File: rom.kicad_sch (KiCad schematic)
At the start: 7 parts, among them U10 28C256, U6 74HC32, U7 74HC14, U8 74HC05, U9 28C256

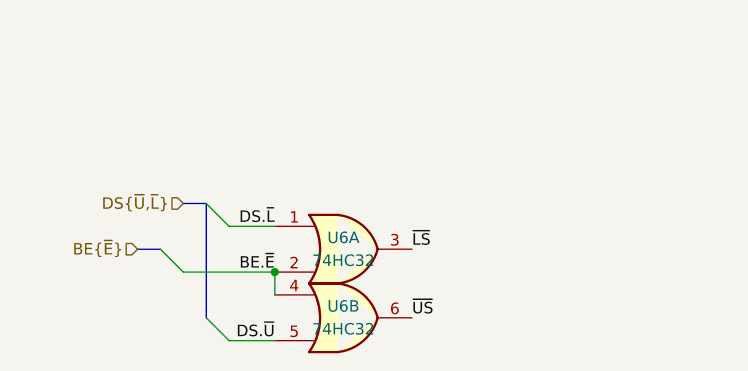
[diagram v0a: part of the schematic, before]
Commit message: finished scheme, footprints not completely assigned yet
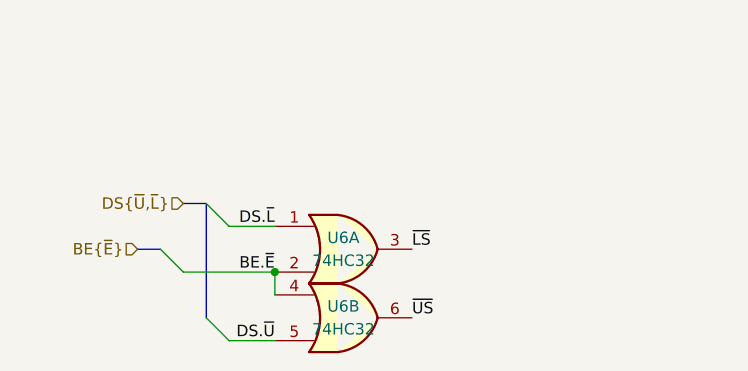
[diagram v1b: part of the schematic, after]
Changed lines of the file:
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@@
 (kicad_sch
-	(version 20231120)
+	(version 20250114)
 	(generator "eeschema")
-	(generator_version "8.0")
+	(generator_version "9.0")
 	(paper "A4")
 	(junction
@@
 	(label "~{US}"
 		(at 83.82 149.86 0)
-		(fields_autoplaced yes)
 		(effects
 			(font
@@
 	(label "DIR.~{R}"
 		(at 142.24 121.92 180)
-		(fields_autoplaced yes)
 		(effects
 			(font
@@
 	(label "A_{14}"
 		(at 205.74 111.76 180)
-		(fields_autoplaced yes)
 		(effects
 			(font
@@
 	(label "A_{12}"
 		(at 142.24 106.68 180)
-		(fields_autoplaced yes)
 		(effects
 			(font
@@
 	(label "A_{9}"
 		(at 205.74 99.06 180)
-		(fields_autoplaced yes)
 		(effects
 			(font
@@
 	(label "~{LS}"
 		(at 142.24 124.46 180)
-		(fields_autoplaced yes)
 		(effects
 			(font
@@
 	(label "D_{3}"
 		(at 162.56 86.36 0)
-		(fields_autoplaced yes)
 		(effects
 			(font
@@
 	(label "A_{7}"
 		(at 142.24 93.98 180)
-		(fields_autoplaced yes)
 		(effects
 			(font
@@
 	(label "BE.~{E}"
 		(at 63.5 76.2 180)
-		(fields_autoplaced yes)
 		(effects
 			(font
@@
 	(label "A_{6}"
 		(at 205.74 91.44 180)
-		(fields_autoplaced yes)
 		(effects
 			(font
@@
 	(label "D_{11}"
 		(at 226.06 86.36 0)
-		(fields_autoplaced yes)
 		(effects
 			(font
@@
 	(label "A_{8}"
 		(at 205.74 96.52 180)
-		(fields_autoplaced yes)
 		(effects
 			(font
@@
 	(label "A_{5}"
 		(at 205.74 88.9 180)
-		(fields_autoplaced yes)
 		(effects
 			(font
@@
 	(label "A_{3}"
 		(at 142.24 83.82 180)
-		(fields_autoplaced yes)
 		(effects
 			(font
@@
 	(label "D_{8}"
 		(at 226.06 78.74 0)
-		(fields_autoplaced yes)
 		(effects
 			(font
@@
 	(label "D_{12}"
 		(at 226.06 88.9 0)
-		(fields_autoplaced yes)
 		(effects
 			(font
@@
 	(label "A_{7}"
 		(at 205.74 93.98 180)
-		(fields_autoplaced yes)
 		(effects
 			(font
@@
 	(label "A_{6}"
 		(at 142.24 91.44 180)
-		(fields_autoplaced yes)
 		(effects
 			(font
@@
 	(label "A_{13}"
 		(at 205.74 109.22 180)
-		(fields_autoplaced yes)
 		(effects
 			(font
@@
 	(label "~{LS}"
 		(at 83.82 142.24 0)
-		(fields_autoplaced yes)
 		(effects
 			(font
@@
 	(label "A_{5}"
 		(at 142.24 88.9 180)
-		(fields_autoplaced yes)
 		(effects
 			(font
@@
 	(label "DIR.~{W}"
 		(at 142.24 119.38 180)
-		(fields_autoplaced yes)
 		(effects
 			(font
@@
 	(label "A_{4}"
 		(at 205.74 86.36 180)
-		(fields_autoplaced yes)
 		(effects
 			(font
@@
 	(label "D_{10}"
 		(at 226.06 83.82 0)
-		(fields_autoplaced yes)
 		(effects
 			(font
@@
 	(label "BE.~{E}"
 		(at 68.58 144.78 180)
-		(fields_autoplaced yes)
 		(effects
 			(font
@@
 	(label "D_{1}"
 		(at 162.56 81.28 0)
-		(fields_autoplaced yes)
 		(effects
 			(font
@@
 	(label "A_{10}"
 		(at 142.24 101.6 180)
-		(fields_autoplaced yes)
 		(effects
 			(font
@@
 	(label "A_{2}"
 		(at 142.24 81.28 180)
-		(fields_autoplaced yes)
 		(effects
 			(font
@@
 	(label "A_{2}"
 		(at 205.74 81.28 180)
-		(fields_autoplaced yes)
 		(effects
 			(font
@@
 	(label "D_{4}"
 		(at 162.56 88.9 0)
-		(fields_autoplaced yes)
 		(effects
 			(font
@@
 	(label "D_{9}"
 		(at 226.06 81.28 0)
-		(fields_autoplaced yes)
 		(effects
 			(font
@@
 	(label "A_{14}"
 		(at 142.24 111.76 180)
-		(fields_autoplaced yes)
 		(effects
 			(font
@@
 	(label "D_{15}"
 		(at 226.06 96.52 0)
-		(fields_autoplaced yes)
 		(effects
 			(font
@@
 	(label "A_{9}"
 		(at 142.24 99.06 180)
-		(fields_autoplaced yes)
 		(effects
 			(font
@@
 	(label "A_{1}"
 		(at 205.74 78.74 180)
-		(fields_autoplaced yes)
 		(effects
 			(font
@@
 	(label "DS.~{L}"
 		(at 68.58 139.7 180)
-		(fields_autoplaced yes)
 		(effects
 			(font
@@
 	(label "DS.~{U}"
 		(at 68.58 152.4 180)
-		(fields_autoplaced yes)
 		(effects
 			(font
@@
 	(label "A_{4}"
 		(at 142.24 86.36 180)
-		(fields_autoplaced yes)
 		(effects
 			(font
@@
 	(label "A_{8}"
 		(at 142.24 96.52 180)
-		(fields_autoplaced yes)
 		(effects
 			(font
@@
 	(label "A_{15}"
 		(at 205.74 114.3 180)
-		(fields_autoplaced yes)
 		(effects
 			(font
@@
 	(label "D_{2}"
 		(at 162.56 83.82 0)
-		(fields_autoplaced yes)
 		(effects
 			(font
@@
 	(label "A_{12}"
 		(at 205.74 106.68 180)
-		(fields_autoplaced yes)
 		(effects
 			(font
@@
 	(label "DIR.~{W}"
 		(at 205.74 119.38 180)
-		(fields_autoplaced yes)
 		(effects
 			(font
@@
 	(label "D_{14}"
 		(at 226.06 93.98 0)
-		(fields_autoplaced yes)
 		(effects
 			(font
@@
 	(label "~{US}"
 		(at 205.74 124.46 180)
-		(fields_autoplaced yes)
 		(effects
 			(font
@@
 	(label "A_{13}"
 		(at 142.24 109.22 180)
-		(fields_autoplaced yes)
 		(effects
 			(font
@@
 	(label "D_{6}"
 		(at 162.56 93.98 0)
-		(fields_autoplaced yes)
 		(effects
 			(font
@@
 	(label "D_{13}"
 		(at 226.06 91.44 0)
-		(fields_autoplaced yes)
 		(effects
 			(font
@@
 	(label "D_{0}"
 		(at 162.56 78.74 0)
-		(fields_autoplaced yes)
 		(effects
 			(font
@@
 	(label "A_{3}"
 		(at 205.74 83.82 180)
-		(fields_autoplaced yes)
 		(effects
 			(font
@@
 	(label "D_{7}"
 		(at 162.56 96.52 0)
-		(fields_autoplaced yes)
 		(effects
 			(font
@@
 	(label "DIR.~{R}"
 		(at 205.74 121.92 180)
-		(fields_autoplaced yes)
 		(effects
 			(font
@@
 	(label "A_{11}"
 		(at 205.74 104.14 180)
-		(fields_autoplaced yes)
 		(effects
 			(font
@@
 	(label "A_{15}"
 		(at 142.24 114.3 180)
-		(fields_autoplaced yes)
 		(effects
 			(font
@@
 	(label "A_{10}"
 		(at 205.74 101.6 180)
-		(fields_autoplaced yes)
 		(effects
 			(font
@@
 	(label "A_{1}"
 		(at 142.24 78.74 180)
-		(fields_autoplaced yes)
 		(effects
 			(font
@@
 	(label "D_{5}"
 		(at 162.56 91.44 0)
-		(fields_autoplaced yes)
 		(effects
 			(font
@@
 	(label "A_{11}"
 		(at 142.24 104.14 180)
-		(fields_autoplaced yes)
 		(effects
 			(font
@@
 		(shape input)
 		(at 53.34 142.24 180)
-		(fields_autoplaced yes)
 		(effects
 			(font
@@
 		(shape bidirectional)
 		(at 234.95 76.2 0)
-		(fields_autoplaced yes)
 		(effects
 			(font
@@
 		(shape input)
 		(at 196.85 76.2 180)
-		(fields_autoplaced yes)
 		(effects
 			(font
@@
 		(shape input)
 		(at 132.08 116.84 180)
-		(fields_autoplaced yes)
 		(effects
 			(font
@@
 		(shape bidirectional)
 		(at 170.18 76.2 0)
-		(fields_autoplaced yes)
 		(effects
 			(font
@@
 		(shape input)
 		(at 53.34 73.66 180)
-		(fields_autoplaced yes)
 		(effects
 			(font
@@
 		(shape input)
 		(at 58.42 137.16 180)
-		(fields_autoplaced yes)
 		(effects
 			(font
@@
 		(shape input)
 		(at 133.35 76.2 180)
-		(fields_autoplaced yes)
 		(effects
 			(font
@@
 		(shape output)
 		(at 101.6 76.2 0)
-		(fields_autoplaced yes)
 		(effects
 			(font
@@
 		(shape input)
 		(at 195.58 116.84 180)
-		(fields_autoplaced yes)
-		(effects
-			(font
+		(effects
+			(font

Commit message: done the pcb layout + added the 1M ram bank project
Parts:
- C1: footprint Capacitor_THT:C_Disc_P2.54mm -> Capacitor_THT:C_Disc_D3.0mm_W1.6mm_P2.54mm
- U10, U9: footprint Package_DIP:DIP-28_W15.24mm_Socket -> Package_DIP:DIP-28_W15.24mm
- U6, U7, U8: footprint Package_DIP:DIP-14_W7.62mm_Socket -> Package_DIP:DIP-14_W7.62mm
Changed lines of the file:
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@@
 			)
 		)
-		(property "Footprint" "Package_DIP:DIP-14_W7.62mm_Socket"
+		(property "Footprint" "Package_DIP:DIP-14_W7.62mm"
 			(at 76.2 142.24 0)
 			(effects
@@
 			)
 		)
-		(property "Footprint" "Package_DIP:DIP-28_W15.24mm_Socket"
+		(property "Footprint" "Package_DIP:DIP-28_W15.24mm"
 			(at 152.4 101.6 0)
 			(effects
@@
 			)
 		)
-		(property "Footprint" "Package_DIP:DIP-14_W7.62mm_Socket"
+		(property "Footprint" "Package_DIP:DIP-14_W7.62mm"
 			(at 71.12 76.2 0)
 			(effects
@@
 			)
 		)
-		(property "Footprint" "Package_DIP:DIP-28_W15.24mm_Socket"
+		(property "Footprint" "Package_DIP:DIP-28_W15.24mm"
 			(at 215.9 101.6 0)
 			(effects
@@
 			)
 		)
-		(property "Footprint" "Capacitor_THT:C_Disc_P2.54mm"
+		(property "Footprint" "Capacitor_THT:C_Disc_D3.0mm_W1.6mm_P2.54mm"
 			(at 86.36 75.2348 0)
 			(effects
@@
 			)
 		)
-		(property "Footprint" "Package_DIP:DIP-14_W7.62mm_Socket"
+		(property "Footprint" "Package_DIP:DIP-14_W7.62mm"
 			(at 76.2 149.86 0)
 			(effects
@@
 			)
 		)
-		(property "Footprint" "Package_DIP:DIP-14_W7.62mm_Socket"
+		(property "Footprint" "Package_DIP:DIP-14_W7.62mm"
 			(at 93.98 76.2 0)
 			(effects

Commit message: [scheme] no major changes
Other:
- moved on the sheet: C1, R4, U6A, U6B, U7B, U8A
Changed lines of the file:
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@@
 	(paper "A4")
 	(junction
-		(at 68.58 144.78)
+		(at 81.28 116.84)
 		(diameter 0)
 		(color 0 0 0 0)
 	)
 	(junction
-		(at 86.36 76.2)
+		(at 81.28 88.9)
 		(diameter 0)
 		(color 0 0 0 0)
@@
 	)
 	(bus_entry
-		(at 60.96 149.86)
+		(at 73.66 121.92)
 		(size 2.54 2.54)
 		(stroke
@@
 	)
 	(bus_entry
-		(at 55.88 142.24)
+		(at 68.58 114.3)
 		(size 2.54 2.54)
 		(stroke
@@
 	)
 	(bus_entry
-		(at 55.88 73.66)
+		(at 50.8 86.36)
 		(size 2.54 2.54)
 		(stroke
@@
 	)
 	(bus_entry
-		(at 60.96 137.16)
+		(at 73.66 109.22)
 		(size 2.54 2.54)
 		(stroke
@@
 	(bus
 		(pts
-			(xy 53.34 142.24) (xy 55.88 142.24)
+			(xy 66.04 114.3) (xy 68.58 114.3)
 		)
 		(stroke
@@
 	(wire
 		(pts
-			(xy 58.42 144.78) (xy 68.58 144.78)
+			(xy 71.12 116.84) (xy 81.28 116.84)
 		)
 		(stroke
@@
 	(bus
 		(pts
-			(xy 53.34 73.66) (xy 55.88 73.66)
+			(xy 48.26 86.36) (xy 50.8 86.36)
 		)
 		(stroke
@@
 	(wire
 		(pts
-			(xy 68.58 144.78) (xy 68.58 147.32)
+			(xy 81.28 116.84) (xy 81.28 119.38)
 		)
 		(stroke
@@
 	(wire
 		(pts
-			(xy 58.42 76.2) (xy 63.5 76.2)
+			(xy 53.34 88.9) (xy 58.42 88.9)
 		)
 		(stroke
@@
 	(wire
 		(pts
-			(xy 63.5 139.7) (xy 68.58 139.7)
+			(xy 76.2 111.76) (xy 81.28 111.76)
 		)
 		(stroke
@@
 	(wire
 		(pts
-			(xy 63.5 152.4) (xy 68.58 152.4)
+			(xy 76.2 124.46) (xy 81.28 124.46)
 		)
 		(stroke
@@
 	(bus
 		(pts
-			(xy 60.96 137.16) (xy 60.96 149.86)
+			(xy 73.66 109.22) (xy 73.66 121.92)
 		)
 		(stroke
@@
 	(bus
 		(pts
-			(xy 58.42 137.16) (xy 60.96 137.16)
+			(xy 71.12 109.22) (xy 73.66 109.22)
 		)
 		(stroke
@@
 	)
 	(label "~{US}"
-		(at 83.82 149.86 0)
+		(at 96.52 121.92 0)
 		(effects
 			(font
@@
 	)
 	(label "BE.~{E}"
-		(at 63.5 76.2 180)
+		(at 58.42 88.9 180)
 		(effects
 			(font
@@
 	)
 	(label "~{LS}"
-		(at 83.82 142.24 0)
+		(at 96.52 114.3 0)
 		(effects
 			(font
@@
 	)
 	(label "BE.~{E}"
-		(at 68.58 144.78 180)
+		(at 81.28 116.84 180)
 		(effects
 			(font
@@
 	)
 	(label "DS.~{L}"
-		(at 68.58 139.7 180)
+		(at 81.28 111.76 180)
 		(effects
 			(font
@@
 	)
 	(label "DS.~{U}"
-		(at 68.58 152.4 180)
+		(at 81.28 124.46 180)
 		(effects
 			(font
@@
 	(hierarchical_label "BE{~{E}}"
 		(shape input)
-		(at 53.34 142.24 180)
+		(at 66.04 114.3 180)
 		(effects
 			(font
@@
 	(hierarchical_label "BE{~{E}}"
 		(shape input)
-		(at 53.34 73.66 180)
+		(at 48.26 86.36 180)
 		(effects
 			(font
@@
 	(hierarchical_label "DS{~{U},~{L}}"
 		(shape input)
-		(at 58.42 137.16 180)
+		(at 71.12 109.22 180)
 		(effects
 			(font
@@
 	(hierarchical_label "DRD"
 		(shape output)
-		(at 101.6 76.2 0)
+		(at 96.52 88.9 0)
 		(effects
 			(font
@@
 	(symbol
 		(lib_id "74xx:74LS32")
-		(at 76.2 142.24 0)
+		(at 88.9 114.3 0)
 		(unit 1)
 		(exclude_from_sim no)
@@
 		(dnp no)
 		(property "Reference" "U6"
-			(at 76.2 140.97 0)
+			(at 88.9 113.03 0)
 			(effects
 				(font
@@
 		)
 		(property "Value" "74HC32"
-			(at 76.2 143.51 0)
+			(at 88.9 115.57 0)
 			(effects
 				(font
@@
 		)
 		(property "Footprint" "Package_DIP:DIP-14_W7.62mm"
-			(at 76.2 142.24 0)
+			(at 88.9 114.3 0)
 			(effects
 				(font
@@
 		)
 		(property "Datasheet" "http://www.ti.com/lit/gpn/sn74LS32"
-			(at 76.2 142.24 0)
+			(at 88.9 114.3 0)
 			(effects
 				(font
@@
 		)
 		(property "Description" "Quad 2-input OR"
-			(at 76.2 142.24 0)
+			(at 88.9 114.3 0)
 			(effects
 				(font
@@
 	(symbol
 		(lib_id "Device:R")
-		(at 86.36 80.01 0)
+		(at 81.28 92.71 0)
 		(mirror y)
 		(unit 1)
@@
 		(dnp no)
 		(property "Reference" "R4"
-			(at 88.9 78.7399 0)
+			(at 83.82 91.4399 0)
 			(effects
 				(font
@@
 		)
 		(property "Value" "20k"
-			(at 88.9 81.2799 0)
+			(at 83.82 93.9799 0)
 			(effects
 				(font
@@
 		)
 		(property "Footprint" "Resistor_THT:R_Axial_DIN0207_L6.3mm_D2.5mm_P2.54mm_Vertical"
-			(at 88.138 80.01 90)
+			(at 83.058 92.71 90)
 			(effects
 				(font
@@
 		)
 		(property "Datasheet" "~"
-			(at 86.36 80.01 0)
+			(at 81.28 92.71 0)
 			(effects
 				(font
@@
 		)
 		(property "Description" "Resistor"
-			(at 86.36 80.01 0)
+			(at 81.28 92.71 0)
 			(effects
 				(font
@@
 	(symbol
 		(lib_id "74xx:74HC14")
-		(at 71.12 76.2 0)
+		(at 66.04 88.9 0)
 		(unit 2)
 		(exclude_from_sim no)
@@
 		(dnp no)
 		(property "Reference" "U7"
-			(at 71.12 74.93 0)
+			(at 66.04 87.63 0)
 			(effects
 				(font
@@
 		)
 		(property "Value" "74HC14"
-			(at 71.12 77.47 0)
+			(at 66.04 90.17 0)
 			(effects
 				(font
@@
 		)
 		(property "Footprint" "Package_DIP:DIP-14_W7.62mm"
-			(at 71.12 76.2 0)
+			(at 66.04 88.9 0)
 			(effects
 				(font
@@
 		)
 		(property "Datasheet" "http://www.ti.com/lit/gpn/sn74HC14"
-			(at 71.12 76.2 0)
+			(at 66.04 88.9 0)
 			(effects
 				(font
@@
 		)
 		(property "Description" "Hex inverter schmitt trigger"
-			(at 71.12 76.2 0)
+			(at 66.04 88.9 0)
 			(effects
 				(font
@@
 	(symbol
 		(lib_id "Device:C")
-		(at 82.55 76.2 90)
+		(at 77.47 88.9 90)
 		(unit 1)
 		(exclude_from_sim no)
@@
 		(dnp no)
 		(property "Reference" "C1"
-			(at 82.55 72.644 90)
+			(at 77.47 85.344 90)
 			(effects
 				(font
@@
 		)
 		(property "Value" "22pF"
-			(at 82.55 79.756 90)
+			(at 77.47 92.456 90)
 			(effects
 				(font
@@
 		)
 		(property "Footprint" "Capacitor_THT:C_Disc_D3.0mm_W1.6mm_P2.54mm"
-			(at 86.36 75.2348 0)
+			(at 81.28 87.9348 0)
 			(effects
 				(font
@@
 		)
 		(property "Datasheet" "~"
-			(at 82.55 76.2 0)
+			(at 77.47 88.9 0)
 			(effects
 				(font
@@
 		)
 		(property "Description" "Unpolarized capacitor"
-			(at 82.55 76.2 0)
+			(at 77.47 88.9 0)
 			(effects
 				(font
@@
 	(symbol
 		(lib_id "power:GND")
-		(at 86.36 83.82 0)
+		(at 81.28 96.52 0)
 		(mirror y)
 		(unit 1)
@@
 		(dnp no)
 		(property "Reference" "#PWR027"
-			(at 86.36 90.17 0)
+			(at 81.28 102.87 0)
 			(effects
 				(font
@@
 		)
 		(property "Value" "GND"
-			(at 86.36 87.884 0)
+			(at 81.28 100.584 0)
 			(effects
 				(font
@@
 		)
 		(property "Footprint" ""
-			(at 86.36 83.82 0)
+			(at 81.28 96.52 0)
 			(effects
 				(font
@@
 		)
 		(property "Datasheet" ""
-			(at 86.36 83.82 0)
+			(at 81.28 96.52 0)
 			(effects
 				(font
@@
 		)
 		(property "Description" "Power symbol creates a global label with name \"GND\" , ground"
-			(at 86.36 83.82 0)
+			(at 81.28 96.52 0)
 			(effects
 				(font
@@
 	(symbol
 		(lib_id "74xx:74LS32")
-		(at 76.2 149.86 0)
+		(at 88.9 121.92 0)
 		(unit 2)
 		(exclude_from_sim no)
@@
 		(dnp no)
 		(property "Reference" "U6"
-			(at 76.2 148.59 0)
+			(at 88.9 120.65 0)
 			(effects
 				(font
@@
 		)
 		(property "Value" "74HC32"
-			(at 76.2 151.13 0)
+			(at 88.9 123.19 0)
 			(effects
 				(font
@@
 		)
 		(property "Footprint" "Package_DIP:DIP-14_W7.62mm"
-			(at 76.2 149.86 0)
+			(at 88.9 121.92 0)
 			(effects
 				(font
@@
 		)
 		(property "Datasheet" "http://www.ti.com/lit/gpn/sn74LS32"
-			(at 76.2 149.86 0)
+			(at 88.9 121.92 0)
 			(effects
 				(font
@@
 		)
 		(property "Description" "Quad 2-input OR"
-			(at 76.2 149.86 0)
+			(at 88.9 121.92 0)
 			(effects
 				(font
@@
 	(symbol
 		(lib_id "74xx:74LS05")
-		(at 93.98 76.2 0)
+		(at 88.9 88.9 0)
 		(unit 1)
 		(exclude_from_sim no)
@@
 		(dnp no)
 		(property "Reference" "U8"
-			(at 93.98 74.676 0)
+			(at 88.9 87.376 0)
 			(effects
 				(font
@@
 		)
 		(property "Value" "74HC05"
-			(at 93.98 77.216 0)
+			(at 88.9 89.916 0)
 			(effects
 				(font
@@
 		)
 		(property "Footprint" "Package_DIP:DIP-14_W7.62mm"
-			(at 93.98 76.2 0)
+			(at 88.9 88.9 0)
 			(effects
 				(font
@@
 		)
 		(property "Datasheet" "http://www.ti.com/lit/gpn/sn74LS05"
-			(at 93.98 76.2 0)
+			(at 88.9 88.9 0)
 			(effects
 				(font
@@
 		)
 		(property "Description" "Inverter Open Collect"
-			(at 93.98 76.2 0)
-			(effects
-				(font
+			(at 88.9 88.9 0)
+			(effects
+				(font

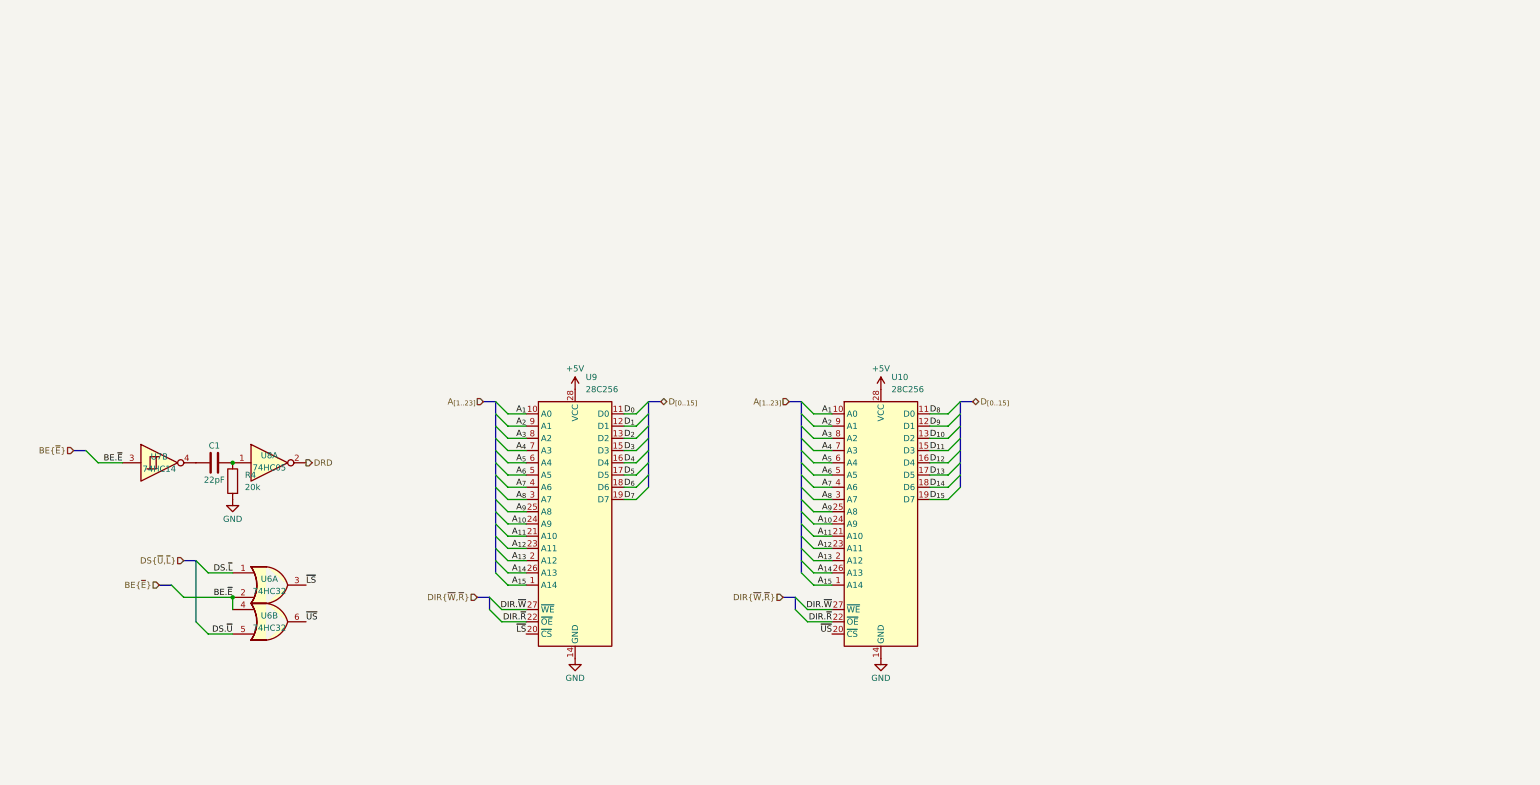
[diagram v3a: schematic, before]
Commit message: first commit: scheme ok [decoder]: 	- new spv. address space [mmu]: 	- removed pidreg 	- switched back to 8Kb mmu rams [ram/peripherals]: 	- added ground pins to connectors [misc]: 	- added DMA support 	- added clock halfer
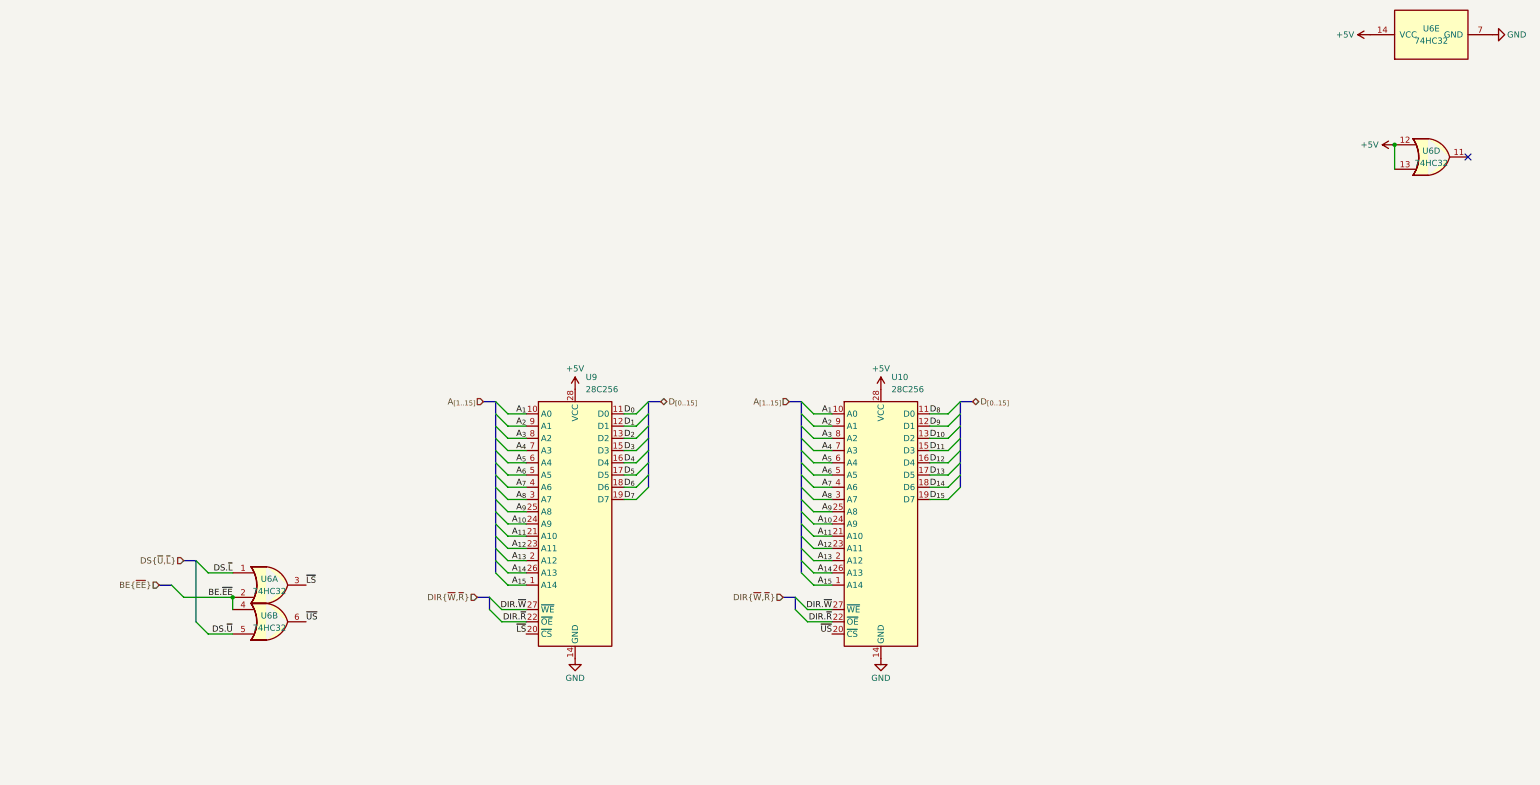
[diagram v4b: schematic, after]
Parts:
- removed C1: 22pF, Capacitor_THT:C_Disc_D3.0mm_W1.6mm_P2.54mm, symbol Device:C
- removed R4: 20k, Resistor_THT:R_Axial_DIN0207_L6.3mm_D2.5mm_P2.54mm_Vertical, symbol Device:R
- removed U7: 74HC14, Package_DIP:DIP-14_W7.62mm, symbol 74xx:74HC14
- removed U8: 74HC05, Package_DIP:DIP-14_W7.62mm, symbol 74xx:74LS05
- added unit 5 of U6
- added unit 4 of U6
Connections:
- net +5V: now also U6.12, U6.13, U6.14 (VCC)
- net GND: now also U6.7 (GND)
- net BE.~{E} renamed BE.~{EE}
- no-connect marks 0 -> 1
